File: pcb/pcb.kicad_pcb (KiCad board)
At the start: 2 copper layers, 109 x 54 mm, 60 parts, among them J1 MALE, J10 TC2030_NL, J101 MALE, J102 FEMALE, J103 MALE, J104 FEMALE, J105 MALE, J106 FEMALE, J107 MALE, J108 FEMALE, J11 STANDOFF, J111 STANDOFF, J112 STANDOFF, J113 STANDOFF, J114 STANDOFF, J12 STANDOFF, J13 STANDOFF, J14 STANDOFF, J2 FEMALE, J3 MALE, J4 FEMALE, J5 MALE, J6 FEMALE, J7 MALE, J8 FEMALE, J9 DTR, Q1 2N3904, SW1 ACTION, SW2 ACTION, SW3 ACTION, SW4 ACTION, U3 ATmega328P-MU, Y1 YSX321SL

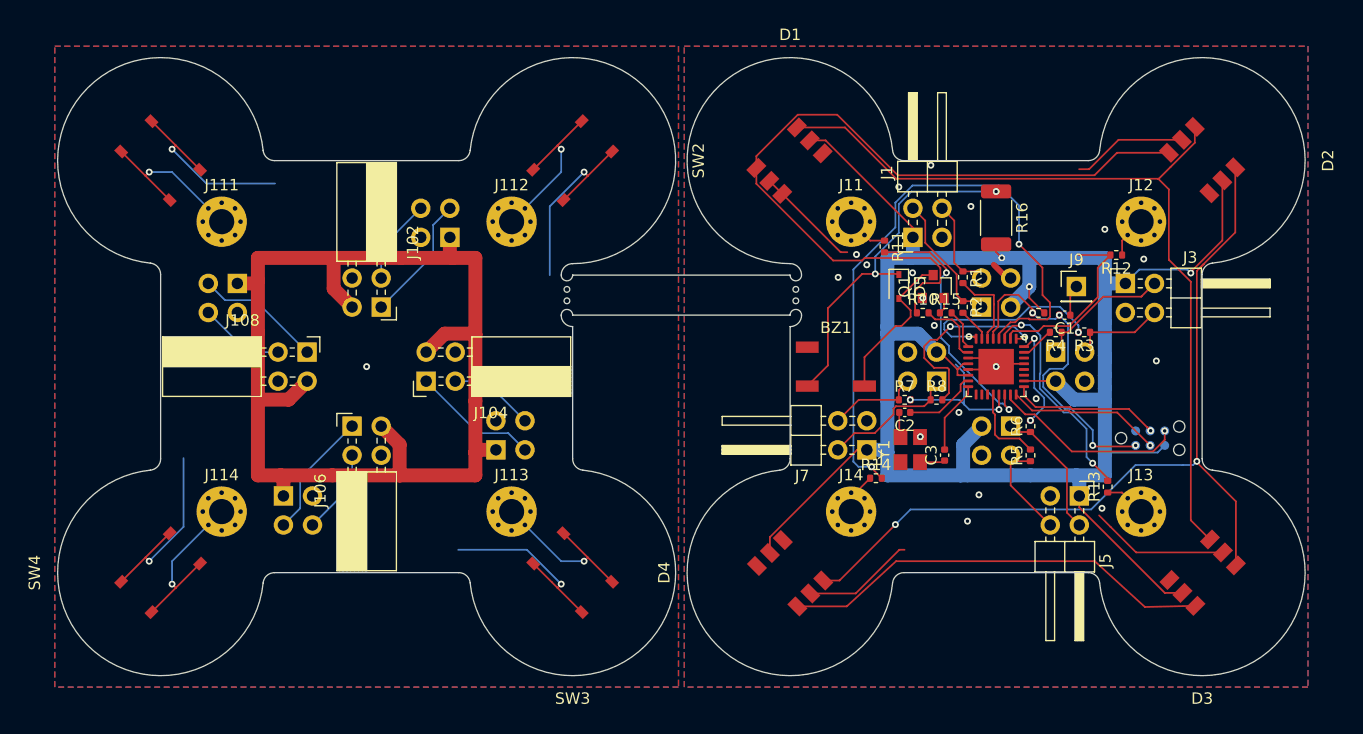
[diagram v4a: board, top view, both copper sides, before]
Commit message: Incorporate JLCPCB tooling holes
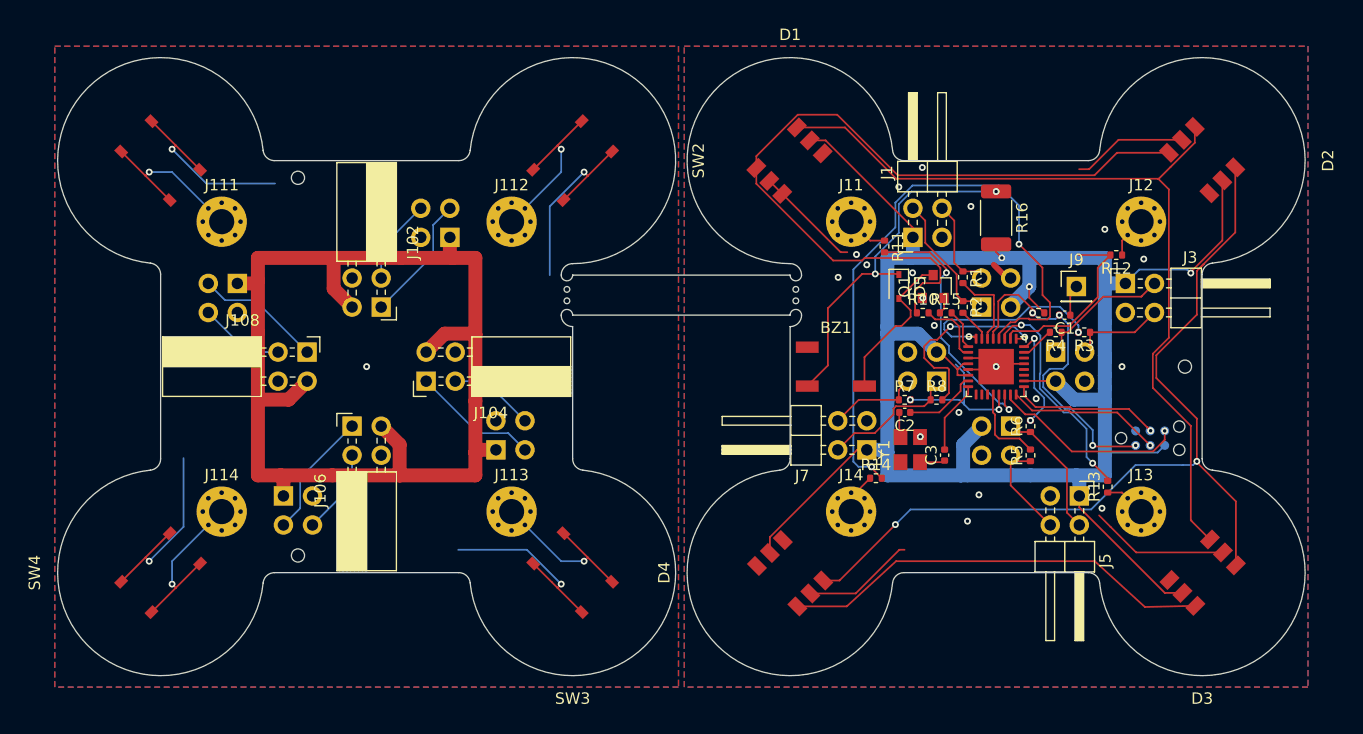
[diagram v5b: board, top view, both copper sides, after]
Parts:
- added jlcpcb-tooling-hole: VAL**, node:JLCPCB-tooling-hole, F.Cu at (192.5, 105.0)
- added jlcpcb-tooling-hole: VAL**, node:JLCPCB-tooling-hole, F.Cu at (115.0, 88.5)
- added jlcpcb-tooling-hole: VAL**, node:JLCPCB-tooling-hole, F.Cu at (115.0, 121.5)
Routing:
- net Net-(D2-Pad3): track 75.1 -> 78.0 mm
- net Net-(D1-Pad3): track 72.7 -> 73.9 mm
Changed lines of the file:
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@@
     (thickness 1)
     (drawings 70)
-    (tracks 579)
+    (tracks 586)
     (zones 0)
-    (modules 60)
+    (modules 63)
     (nets 70)
   )
@@
   )
   (layers
-    (0 F.Cu signal hide)
+    (0 F.Cu signal)
     (31 B.Cu signal)
     (32 B.Adhes user hide)
@@
     (add_net "Net-(U3-Pad9)")
   )
+  (module node:JLCPCB-tooling-hole (layer F.Cu)
+    (at 192.5 105)
+    (descr https://support.jlcpcb.com/article/92-how-to-add-tooling-holes-for-smt-assembly-order)
+    (attr smd)
+    (fp_text reference jlcpcb-tooling-hole (at 0 1.524) (layer F.SilkS) hide
+      (effects (font (size 1 1) (thickness 0.2)))
+    )
+    (fp_text value VAL** (at 0 -1.524) (layer F.SilkS) hide
+      (effects (font (size 1 1) (thickness 0.2)))
+    )
+    (pad "" np_thru_hole circle (at 0 0) (size 1.152 1.152) (drill 1.152) (layers *.Cu *.Mask)
+      (solder_mask_margin 0.074) (clearance 0.124))
+  )
+  (module node:JLCPCB-tooling-hole (layer F.Cu)
+    (at 115 88.5)
+    (descr https://support.jlcpcb.com/article/92-how-to-add-tooling-holes-for-smt-assembly-order)
+    (attr smd)
+    (fp_text reference jlcpcb-tooling-hole (at 0 1.524) (layer F.SilkS) hide
+      (effects (font (size 1 1) (thickness 0.2)))
+    )
+    (fp_text value VAL** (at 0 -1.524) (layer F.SilkS) hide
+      (effects (font (size 1 1) (thickness 0.2)))
+    )
+    (pad "" np_thru_hole circle (at 0 0) (size 1.152 1.152) (drill 1.152) (layers *.Cu *.Mask)
+      (solder_mask_margin 0.074) (clearance 0.124))
+  )
+  (module node:JLCPCB-tooling-hole (layer F.Cu)
+    (at 115 121.5)
+    (descr https://support.jlcpcb.com/article/92-how-to-add-tooling-holes-for-smt-assembly-order)
+    (attr smd)
+    (fp_text reference jlcpcb-tooling-hole (at 0 1.524) (layer F.SilkS) hide
+      (effects (font (size 1 1) (thickness 0.2)))
+    )
+    (fp_text value VAL** (at 0 -1.524) (layer F.SilkS) hide
+      (effects (font (size 1 1) (thickness 0.2)))
+    )
+    (pad "" np_thru_hole circle (at 0 0) (size 1.152 1.152) (drill 1.152) (layers *.Cu *.Mask)
+      (solder_mask_margin 0.074) (clearance 0.124))
+  )
   (module node:bottom-leaf (layer F.Cu)
     (at 194 87 270)
@@
       (effects (font (size 1 1) (thickness 0.15)))
     )
-    (pad 2 smd roundrect (at 2.3125 0 270) (size 1.225 2.65) (layers F.Cu F.Paste F.Mask) (roundrect_rratio 0.204082)
+    (pad 2 smd roundrect (at 2.3125 0 270) (size 1.225 2.65) (layers F.Cu F.Paste F.Mask) (roundrect_rratio 0.2040816326530612)
       (net 33 +5VB))
-    (pad 1 smd roundrect (at -2.3125 0 270) (size 1.225 2.65) (layers F.Cu F.Paste F.Mask) (roundrect_rratio 0.204082)
+    (pad 1 smd roundrect (at -2.3125 0 270) (size 1.225 2.65) (layers F.Cu F.Paste F.Mask) (roundrect_rratio 0.2040816326530612)
       (net 52 "Net-(BZ1-Pad1)"))
     (model ${KISYS3DMOD}/Resistor_SMD.3dshapes/R_2010_5025Metric.wrl
@@
   (segment (start 190.166589 88.583411) (end 190.215021 88.583411) (width 0.1524) (layer F.Cu) (net 11))
   (segment (start 167.277345 88.583411) (end 190.166589 88.583411) (width 0.1524) (layer F.Cu) (net 11))
-  (segment (start 191.094601 89.511423) (end 191.094601 95.65939) (width 0.1524) (layer F.Cu) (net 11))
   (segment (start 190.166589 88.583411) (end 191.094601 89.511423) (width 0.1524) (layer F.Cu) (net 11))
-  (segment (start 193.01142 118.425886) (end 194.686396 120.100862) (width 0.1524) (layer F.Cu) (net 11))
-  (segment (start 193.01142 97.576209) (end 193.01142 118.425886) (width 0.1524) (layer F.Cu) (net 11))
-  (segment (start 191.094601 95.65939) (end 193.01142 97.576209) (width 0.1524) (layer F.Cu) (net 11))
+  (segment (start 193.01142 118.425886) (end 193.092767 118.507233) (width 0.1524) (layer F.Cu) (net 11))
+  (segment (start 193.01142 110.174046) (end 193.01142 118.425886) (width 0.1524) (layer F.Cu) (net 11))
+  (segment (start 189.69519 103.873744) (end 189.69519 106.857816) (width 0.1524) (layer F.Cu) (net 11))
+  (segment (start 191.094601 102.474333) (end 189.69519 103.873744) (width 0.1524) (layer F.Cu) (net 11))
+  (segment (start 189.69519 106.857816) (end 193.01142 110.174046) (width 0.1524) (layer F.Cu) (net 11))
+  (segment (start 191.094601 89.511423) (end 191.094601 102.474333) (width 0.1524) (layer F.Cu) (net 11))
+  (segment (start 193.092767 118.507233) (end 194.686396 120.100862) (width 0.1524) (layer F.Cu) (net 11))
   (segment (start 196.899138 87.586396) (end 196.899138 93.271106) (width 0.1524) (layer F.Cu) (net 12))
   (via (at 167.2 118.8) (size 0.6) (drill 0.3) (layers F.Cu B.Cu) (net 12))
@@
   (segment (start 193.540021 113.36481) (end 196.949138 116.773927) (width 0.1524) (layer F.Cu) (net 12))
   (segment (start 193.540021 113.273315) (end 193.540021 113.36481) (width 0.1524) (layer F.Cu) (net 12))
-  (segment (start 193.540021 96.630223) (end 194.135122 96.035122) (width 0.1524) (layer F.Cu) (net 12))
-  (segment (start 193.540021 113.273315) (end 193.540021 96.630223) (width 0.1524) (layer F.Cu) (net 12))
   (segment (start 194.135122 96.035122) (end 193.741068 96.429176) (width 0.1524) (layer F.Cu) (net 12))
   (segment (start 196.899138 93.271106) (end 194.135122 96.035122) (width 0.1524) (layer F.Cu) (net 12))
+  (segment (start 193.540021 96.630223) (end 194.135122 96.035122) (width 0.1524) (layer F.Cu) (net 12))
+  (segment (start 193.540021 100.459979) (end 193.540021 96.630223) (width 0.1524) (layer F.Cu) (net 12))
+  (segment (start 190 104) (end 193.540021 100.459979) (width 0.1524) (layer F.Cu) (net 12))
+  (segment (start 193.540021 109.540021) (end 190 106) (width 0.1524) (layer F.Cu) (net 12))
+  (segment (start 190 106) (end 190 104) (width 0.1524) (layer F.Cu) (net 12))
+  (segment (start 193.540021 113.273315) (end 193.540021 109.540021) (width 0.1524) (layer F.Cu) (net 12))
   (segment (start 162.949138 125.949138) (end 158.636396 125.949138) (width 0.1524) (layer F.Cu) (net 13))
   (segment (start 167.258932 122) (end 162.949138 125.949138) (width 0.1524) (layer F.Cu) (net 13))
@@
   (via (at 179.5 107.8) (size 0.6) (drill 0.3) (layers F.Cu B.Cu) (net 34))
   (via (at 163.8 95.2) (size 0.6) (drill 0.3) (layers F.Cu B.Cu) (net 34))
-  (via (at 190 104.5) (size 0.6) (drill 0.3) (layers F.Cu B.Cu) (net 34))
+  (via (at 187 105) (size 0.6) (drill 0.3) (layers F.Cu B.Cu) (net 34))
   (via (at 188.9 95.6) (size 0.6) (drill 0.3) (layers F.Cu B.Cu) (net 34))
   (segment (start 192.232233 85.182233) (end 186.696478 85.182233) (width 0.1524) (layer F.Cu) (net 34))
@@
   (segment (start 177.27 97.26) (end 176.96 97.26) (width 0.508) (layer F.Cu) (net 34))
   (segment (start 176.96 97.26) (end 175.8 96.1) (width 0.508) (layer F.Cu) (net 34))
-  (via (at 170.3 87.4) (size 0.6) (drill 0.3) (layers F.Cu B.Cu) (net 34))
+  (via (at 169.55 87.6) (size 0.6) (drill 0.3) (layers F.Cu B.Cu) (net 34))
   (segment (start 187.01 93.99) (end 188.666 92.334) (width 0.1524) (layer F.Cu) (net 35))
   (segment (start 187.01 95.25) (end 187.01 93.99) (width 0.1524) (layer F.Cu) (net 35))

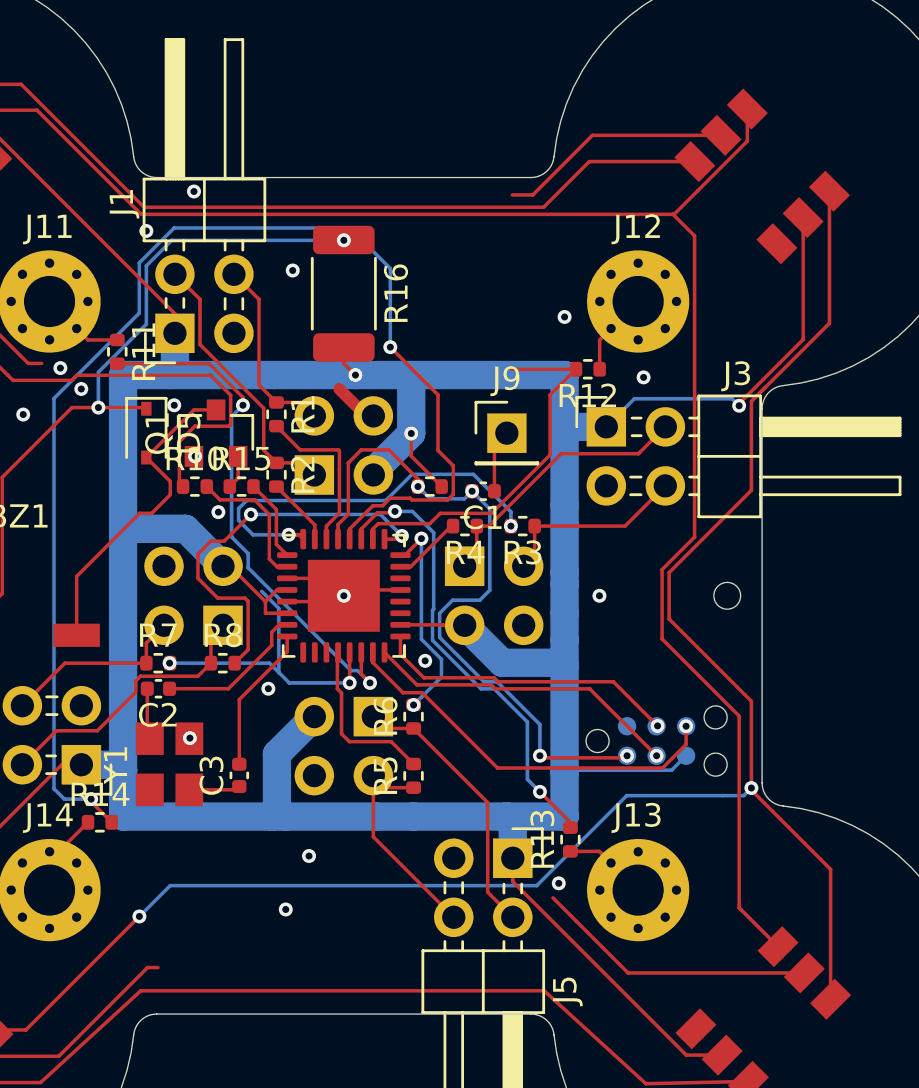
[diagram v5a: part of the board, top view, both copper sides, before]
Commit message: Fix: Non connected GNDB areas
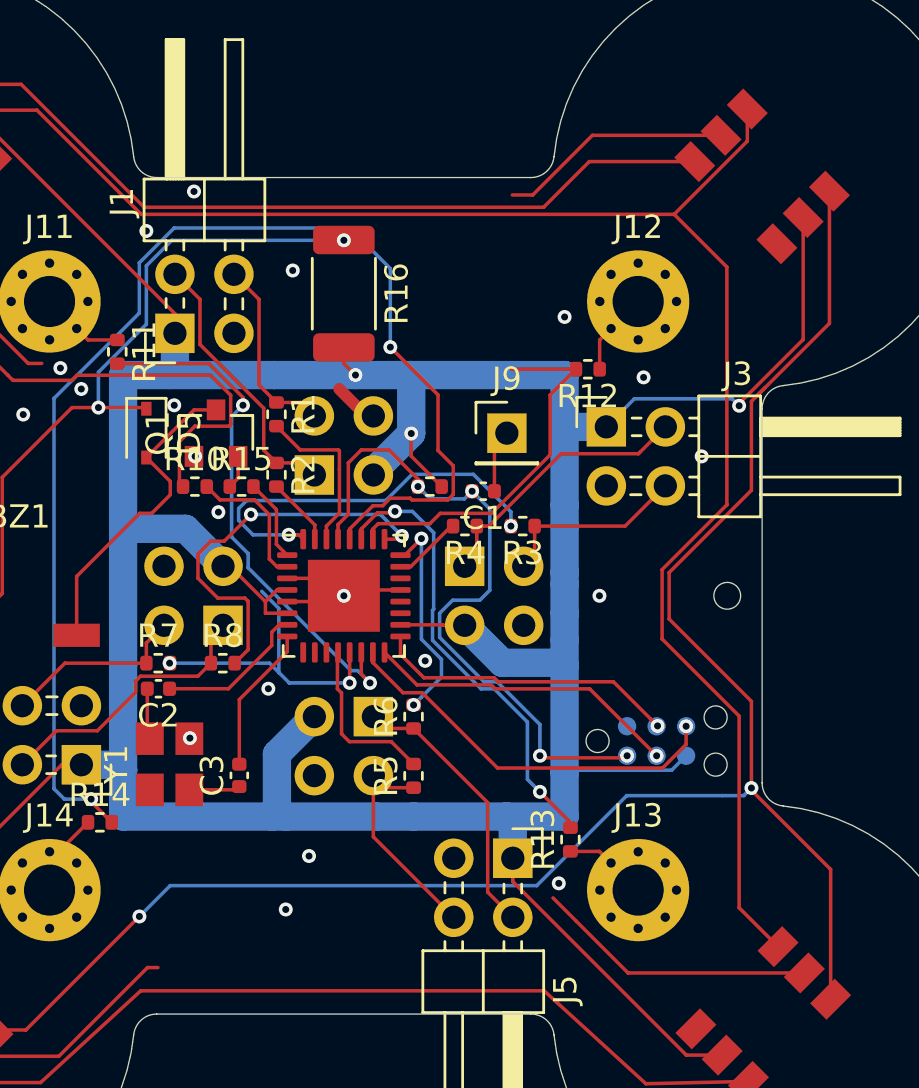
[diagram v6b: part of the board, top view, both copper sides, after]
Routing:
- net Net-(D1-Pad3): track 73.9 -> 75.0 mm
- net GNDB: vias 19 -> 20
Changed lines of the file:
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@@
     (thickness 1)
     (drawings 70)
-    (tracks 586)
+    (tracks 585)
     (zones 0)
     (modules 63)
@@
   (segment (start 173.1 100.3) (end 174.75 101.95) (width 0.1524) (layer F.Cu) (net 4))
   (segment (start 193.363604 85.434828) (end 193.363604 84.050862) (width 0.1524) (layer F.Cu) (net 11))
-  (segment (start 191.234692 87.56374) (end 193.363604 85.434828) (width 0.1524) (layer F.Cu) (net 11))
+  (segment (start 190.215021 88.583411) (end 193.363604 85.434828) (width 0.1524) (layer F.Cu) (net 11))
+  (segment (start 167.277345 88.583411) (end 190.215021 88.583411) (width 0.1524) (layer F.Cu) (net 11))
   (segment (start 162.794796 84.100862) (end 167.277345 88.583411) (width 0.1524) (layer F.Cu) (net 11))
-  (segment (start 190.215021 88.583411) (end 191.234692 87.56374) (width 0.1524) (layer F.Cu) (net 11))
   (segment (start 158.586396 84.100862) (end 162.794796 84.100862) (width 0.1524) (layer F.Cu) (net 11))
-  (segment (start 190.166589 88.583411) (end 190.215021 88.583411) (width 0.1524) (layer F.Cu) (net 11))
-  (segment (start 167.277345 88.583411) (end 190.166589 88.583411) (width 0.1524) (layer F.Cu) (net 11))
-  (segment (start 190.166589 88.583411) (end 191.094601 89.511423) (width 0.1524) (layer F.Cu) (net 11))
-  (segment (start 193.01142 118.425886) (end 193.092767 118.507233) (width 0.1524) (layer F.Cu) (net 11))
-  (segment (start 193.01142 110.174046) (end 193.01142 118.425886) (width 0.1524) (layer F.Cu) (net 11))
-  (segment (start 189.69519 103.873744) (end 189.69519 106.857816) (width 0.1524) (layer F.Cu) (net 11))
-  (segment (start 191.094601 102.474333) (end 189.69519 103.873744) (width 0.1524) (layer F.Cu) (net 11))
-  (segment (start 189.69519 106.857816) (end 193.01142 110.174046) (width 0.1524) (layer F.Cu) (net 11))
-  (segment (start 191.094601 89.511423) (end 191.094601 102.474333) (width 0.1524) (layer F.Cu) (net 11))
-  (segment (start 193.092767 118.507233) (end 194.686396 120.100862) (width 0.1524) (layer F.Cu) (net 11))
+  (segment (start 192.48282 90.85121) (end 190.215021 88.583411) (width 0.1524) (layer F.Cu) (net 11))
+  (segment (start 192.48282 101.08282) (end 192.48282 90.85121) (width 0.1524) (layer F.Cu) (net 11))
+  (segment (start 189.69519 106.857816) (end 189.69519 103.873744) (width 0.1524) (layer F.Cu) (net 11))
+  (segment (start 192.484467 101.084467) (end 192.48282 101.08282) (width 0.1524) (layer F.Cu) (net 11))
+  (segment (start 193.01142 110.174046) (end 189.69519 106.857816) (width 0.1524) (layer F.Cu) (net 11))
+  (segment (start 189.69519 103.873744) (end 192.484467 101.084467) (width 0.1524) (layer F.Cu) (net 11))
+  (segment (start 193.01142 118.425886) (end 193.01142 110.174046) (width 0.1524) (layer F.Cu) (net 11))
+  (segment (start 194.686396 120.100862) (end 193.01142 118.425886) (width 0.1524) (layer F.Cu) (net 11))
   (segment (start 196.899138 87.586396) (end 196.899138 93.271106) (width 0.1524) (layer F.Cu) (net 12))
   (via (at 167.2 118.8) (size 0.6) (drill 0.3) (layers F.Cu B.Cu) (net 12))
@@
   (segment (start 176.96 97.26) (end 175.8 96.1) (width 0.508) (layer F.Cu) (net 34))
   (via (at 169.55 87.6) (size 0.6) (drill 0.3) (layers F.Cu B.Cu) (net 34))
+  (via (at 191.4 99) (size 0.6) (drill 0.3) (layers F.Cu B.Cu) (net 34))
   (segment (start 187.01 93.99) (end 188.666 92.334) (width 0.1524) (layer F.Cu) (net 35))
   (segment (start 187.01 95.25) (end 187.01 93.99) (width 0.1524) (layer F.Cu) (net 35))
